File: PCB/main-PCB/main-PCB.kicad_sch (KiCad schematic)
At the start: 36 parts, among them Q1 SSM6J214FE, Q2 Q_NMOS_GSD, U1 LIS2DU12TR, U2 STM32U031K4Ux

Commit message: -PCB jumper change
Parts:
- removed R1: 0, Resistor_SMD:R_0402_1005Metric, symbol Device:R
- added JP1: SolderJumper_2_Open, Jumper:SolderJumper-2_P1.3mm_Open_RoundedPad1.0x1.5mm, symbol Jumper:SolderJumper_2_Open
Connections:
- net VCC: now also JP1.2 (B)
- net at Q1.1 (D), Q1.2 (D), Q1.5 (D)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: now also JP1.1 (A)
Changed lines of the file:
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@@
+	(wire
+		(pts
+			(xy 69.85 44.45) (xy 71.12 44.45)
+		)
+		(stroke
+			(width 0)
+			(type default)
+		)
+	)
 	(wire
 		(pts
@@
 	(wire
 		(pts
+			(xy 58.42 44.45) (xy 59.69 44.45)
+		)
+		(stroke
+			(width 0)
+			(type default)
+		)
+	)
+	(wire
+		(pts
 			(xy 36.83 157.48) (xy 36.83 156.21)
 		)
@@
 	(wire
 		(pts
-			(xy 68.58 44.45) (xy 71.12 44.45)
-		)
-		(stroke
-			(width 0)
-			(type default)
-		)
-	)
-	(wire
-		(pts
 			(xy 264.16 99.06) (xy 276.86 99.06)
 		)
@@
 		(pts
 			(xy 71.12 55.88) (xy 69.85 55.88)
-		)
-		(stroke
-			(width 0)
-			(type default)
-		)
-	)
-	(wire
-		(pts
-			(xy 60.96 44.45) (xy 58.42 44.45)
 		)
 		(stroke
@@
 	)
 	(symbol
+		(lib_id "Jumper:SolderJumper_2_Open")
+		(at 64.77 44.45 0)
+		(unit 1)
+		(body_style 1)
+		(exclude_from_sim no)
+		(in_bom no)
+		(on_board yes)
+		(in_pos_files yes)
+		(dnp no)
+		(property "Reference" "JP1"
+			(at 64.77 41.91 0)
+			(show_name no)
+			(do_not_autoplace no)
+			(effects
+				(font
+					(size 1.27 1.27)
+				)
+			)
+		)
+		(property "Value" "SolderJumper_2_Open"
+			(at 64.77 40.64 0)
+			(hide yes)
+			(show_name no)
+			(do_not_autoplace no)
+			(effects
+				(font
+					(size 1.27 1.27)
+				)
+			)
+		)
+		(property "Footprint" "Jumper:SolderJumper-2_P1.3mm_Open_RoundedPad1.0x1.5mm"
+			(at 64.77 44.45 0)
+			(hide yes)
+			(show_name no)
+			(do_not_autoplace no)
+			(effects
+				(font
+					(size 1.27 1.27)
+				)
+			)
+		)
+		(property "Datasheet" ""
+			(at 64.77 52.07 0)
+			(hide yes)
+			(show_name no)
+			(do_not_autoplace no)
+			(effects
+				(font
+					(size 1.27 1.27)
+				)
+			)
+		)
+		(property "Description" "Solder Jumper, 2-pole, open"
+			(at 64.77 49.53 0)
+			(hide yes)
+			(show_name no)
+			(do_not_autoplace no)
+			(effects
+				(font
+					(size 1.27 1.27)
+				)
+			)
+		)
+		(pin "2"
+		)
+		(pin "1"
+		)
+		(instances
+			(project "main-PCB"
+				(path "/05d84283-74ff-469f-a29b-6104f656f1bf"
+					(reference "JP1")
+					(unit 1)
+				)
+			)
+		)
+	)
+	(symbol
 		(lib_id "power:GND")
 		(at 64.77 67.31 0)
@@
 					(unit 1)
 				)
-			)
-		)
-	)
-	(symbol
-		(lib_id "Device:R")
-		(at 64.77 44.45 270)
-		(mirror x)
-		(unit 1)
-		(body_style 1)
-		(exclude_from_sim no)
-		(in_bom yes)
-		(on_board yes)
-		(in_pos_files yes)
-		(dnp yes)
-		(property "Reference" "R1"
-			(at 63.5 39.624 90)
-			(show_name no)
-			(do_not_autoplace no)
-			(effects
-				(font
-					(size 1.27 1.27)
-				)
-				(justify left)
-			)
-		)
-		(property "Value" "0"
-			(at 63.5001 41.91 90)
-			(show_name no)
-			(do_not_autoplace no)
-			(effects
-				(font
-					(size 1.27 1.27)
-				)
-				(justify left)
-			)
-		)
-		(property "Footprint" "Resistor_SMD:R_0402_1005Metric"
-			(at 64.77 46.228 90)
-			(hide yes)
-			(show_name no)
-			(do_not_autoplace no)
-			(effects
-				(font
-					(size 1.27 1.27)
-				)
-			)
-		)
-		(property "Datasheet" ""
-			(at 64.77 44.45 0)
-			(hide yes)
-			(show_name no)
-			(do_not_autoplace no)
-			(effects
-				(font
-					(size 1.27 1.27)
-				)
-			)
-		)
-		(property "Description" "Resistor"
-			(at 64.77 44.45 0)
-			(hide yes)
-			(show_name no)
-			(do_not_autoplace no)
-			(effects
-				(font
-					(size 1.27 1.27)
-				)
-			)
-		)
-		(pin "2"
-		)
-		(pin "1"
-		)
-		(instances
-			(project "main-PCB"
-				(path "/05d84283-74ff-469f-a29b-6104f656f1bf"
-					(reference "R1")
-					(unit 1)
-				)

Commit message: Improved error handling in LIS2 sleep function. Changed pulldowns Added jumpers to PCB
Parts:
- added JP2: SolderJumper_2_Bridged, Jumper:SolderJumper-2_P1.3mm_Bridged_RoundedPad1.0x1.5mm, symbol Jumper:SolderJumper_2_Bridged
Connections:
- net VCC: now also JP2.1 (A); no longer C1.1, C2.1, U1.9 (VDD)
- new net: C1.1, C2.1, JP2.2 (B), U1.9 (VDD)
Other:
- moved on the sheet: C1, C2, C3, C4, C5, C6, C7, C8, C9, TP10, TP11, TP12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

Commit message: Updated resistor value Improved LIS init
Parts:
- R2: value 10M -> 20M
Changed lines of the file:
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@@
 			)
 		)
-		(property "Value" "10M"
+		(property "Value" "20M"
 			(at 73.66 62.2299 0)
 			(show_name no)

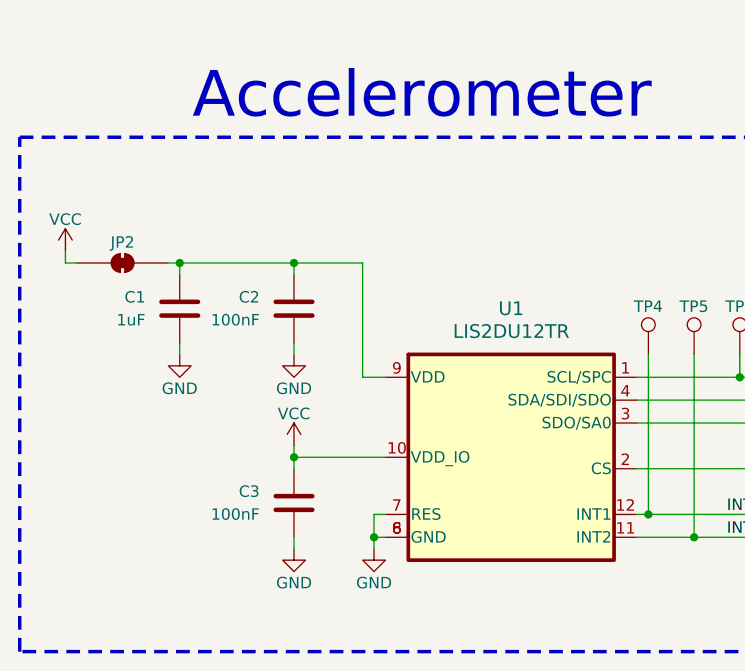
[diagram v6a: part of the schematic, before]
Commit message: -changed accelerometer model
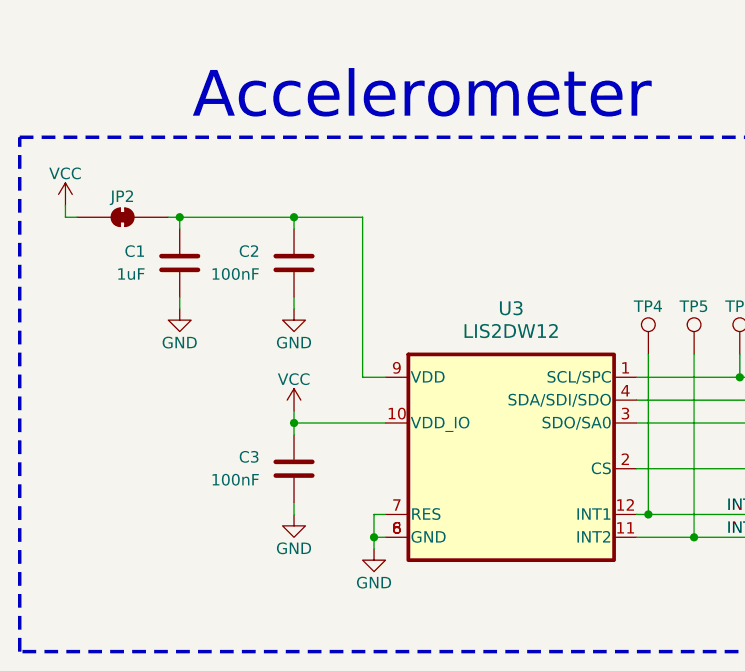
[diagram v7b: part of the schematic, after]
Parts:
- removed U1: LIS2DU12TR, EN_Designs-Footprints:LIS2DU12, symbol EN_Designs-Symbols:LIS2DU12TR
- added U3: LIS2DW12, EN_Designs-Footprints:LIS2DW12, symbol EN_Designs-Symbols:LIS2DW12
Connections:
- net CS: now also U3.2 (CS)
- net GND: now also U3.6 (GND), U3.7 (RES), U3.8 (GND)
- net INT1: now also U3.12 (INT1)
- net INT2: now also U3.11 (INT2)
- net MISO: now also U3.3 (SDO/SA0)
- net MOSI: now also U3.4 (SDA/SDI/SDO)
- net SCLK: now also U3.1 (SCL/SPC)
- net VCC: now also U3.10 (VDD_IO)
- net at C1.1, C2.1, JP2.2 (B): now also U3.9 (VDD)
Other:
- moved on the sheet: C1, C2, C3, JP2
